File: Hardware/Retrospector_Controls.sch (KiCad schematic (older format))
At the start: 23 parts, among them J1 Audio_In_L, J10 Feedback_CV, J11 Audio_In_R, J12 Audio_Out_R, J13 Audio_Out_L, J2 Delay_CV_L, J3 Conn_01x08_Female, J4 Conn_01x08_Female, J5 Conn_01x08_Female, J6 Conn_01x08_Female, J7 Mix_CV, J8 Delay_CV_R, J9 Clock

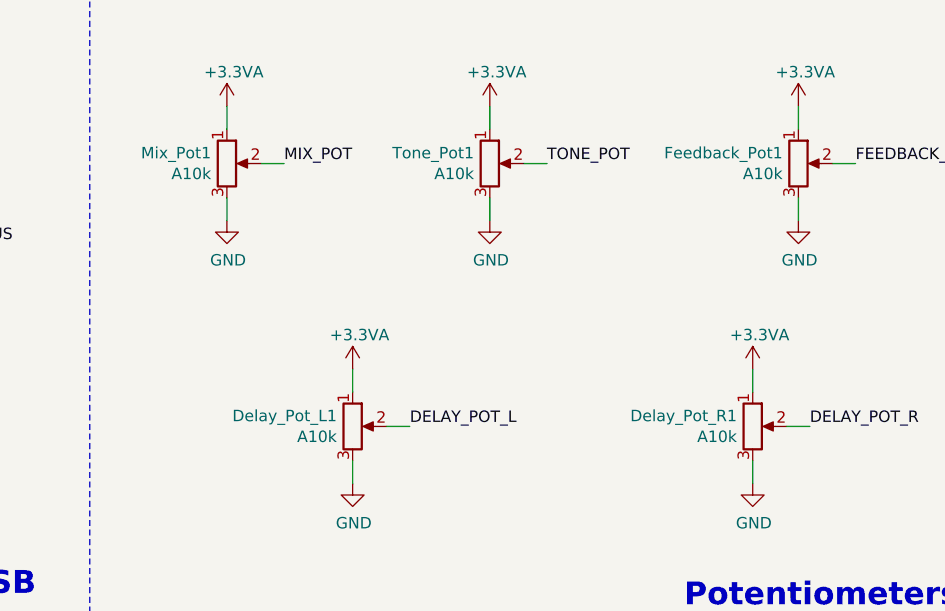
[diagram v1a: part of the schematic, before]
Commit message: Started updating schematics and pcb layout for rev 2 changes; updated and tested clock pin to use production assignment
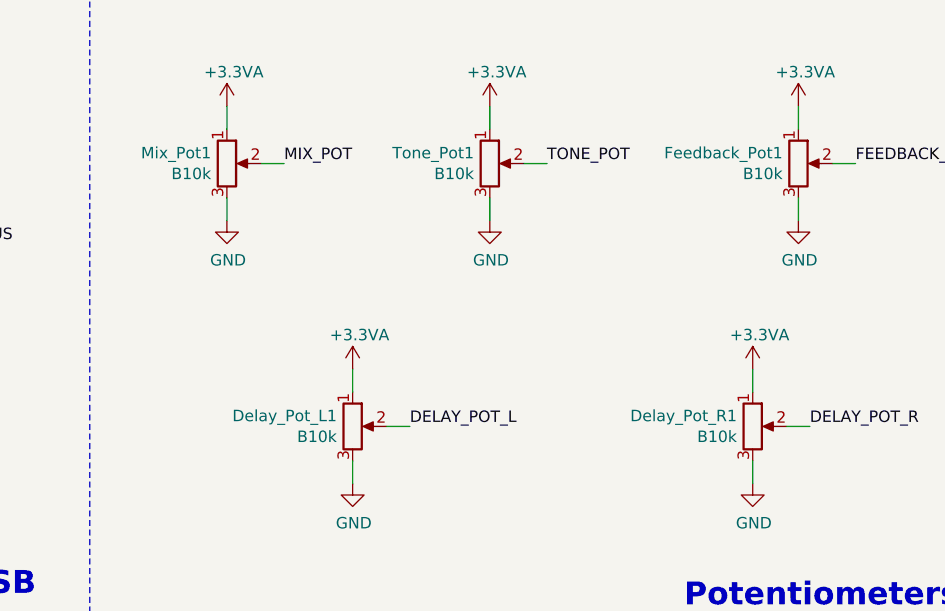
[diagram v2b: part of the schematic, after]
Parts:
- Delay_Pot_L1, Delay_Pot_R1, Feedback_Pot1, Mix_Pot1, Tone_Pot1: value A10k -> B10k
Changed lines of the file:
@@
 P 7800 4400
 F 0 "Mix_Pot1" H 7731 4446 50  0000 R CNN
-F 1 "A10k" H 7731 4355 50  0000 R CNN
+F 1 "B10k" H 7731 4355 50  0000 R CNN
 F 2 "Custom_Footprints:Alpha_9mm_Potentiometer" H 7800 4400 50  0001 C CNN
 F 3 "~" H 7800 4400 50  0001 C CNN
@@
 P 8950 4400
 F 0 "Tone_Pot1" H 8881 4446 50  0000 R CNN
-F 1 "A10k" H 8881 4355 50  0000 R CNN
+F 1 "B10k" H 8881 4355 50  0000 R CNN
 F 2 "Custom_Footprints:Alpha_9mm_Potentiometer" H 8950 4400 50  0001 C CNN
 F 3 "~" H 8950 4400 50  0001 C CNN
@@
 P 10300 4400
 F 0 "Feedback_Pot1" H 10231 4446 50  0000 R CNN
-F 1 "A10k" H 10231 4355 50  0000 R CNN
+F 1 "B10k" H 10231 4355 50  0000 R CNN
 F 2 "Custom_Footprints:Alpha_9mm_Potentiometer" H 10300 4400 50  0001 C CNN
 F 3 "~" H 10300 4400 50  0001 C CNN
@@
 P 8350 5550
 F 0 "Delay_Pot_L1" H 8281 5596 50  0000 R CNN
-F 1 "A10k" H 8281 5505 50  0000 R CNN
+F 1 "B10k" H 8281 5505 50  0000 R CNN
 F 2 "Custom_Footprints:Alpha_9mm_Potentiometer" H 8350 5550 50  0001 C CNN
 F 3 "~" H 8350 5550 50  0001 C CNN
@@
 P 10100 5550
 F 0 "Delay_Pot_R1" H 10031 5596 50  0000 R CNN
-F 1 "A10k" H 10031 5505 50  0000 R CNN
+F 1 "B10k" H 10031 5505 50  0000 R CNN
 F 2 "Custom_Footprints:Alpha_9mm_Potentiometer" H 10100 5550 50  0001 C CNN
 F 3 "~" H 10100 5550 50  0001 C CNN

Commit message: Started updating schematics for new revision
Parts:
- added D3: LED_LEFT, LEDs:LED_D5.0mm-4, symbol Device:LED_RABG
- added D4: LED_RIGHT, LEDs:LED_D5.0mm-4, symbol Device:LED_RABG
- added D5: LED_FILTER, LEDs:LED_D5.0mm-4, symbol Device:LED_RABG
- added J14: Filter, Custom_Footprints:THONKICONN_hole, symbol thonkiconn:AudioJack2_Ground_Switch
- added R1, R2, R3: 1k2, Resistors_SMD:R_0603_HandSoldering, symbol Device:R_Small
- added U1: TB62781FNG, Housings_SSOP:SSOP-20_4.4x6.5mm_Pitch0.65mm, symbol TB62781FNG:TB62781FNG
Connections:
- net labels added: +3.3V, +5V, FILTER_CV, LED_I2C_CLK, LED_I2C_DATA
- net labels removed: USB_DM, USB_DP, USB_VBUS
- wire segments 77 -> 126
- no-connect marks 5 -> 2
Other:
- note added: "LED Controller"
- note removed: "USB"
- moved on the sheet: J5, J6

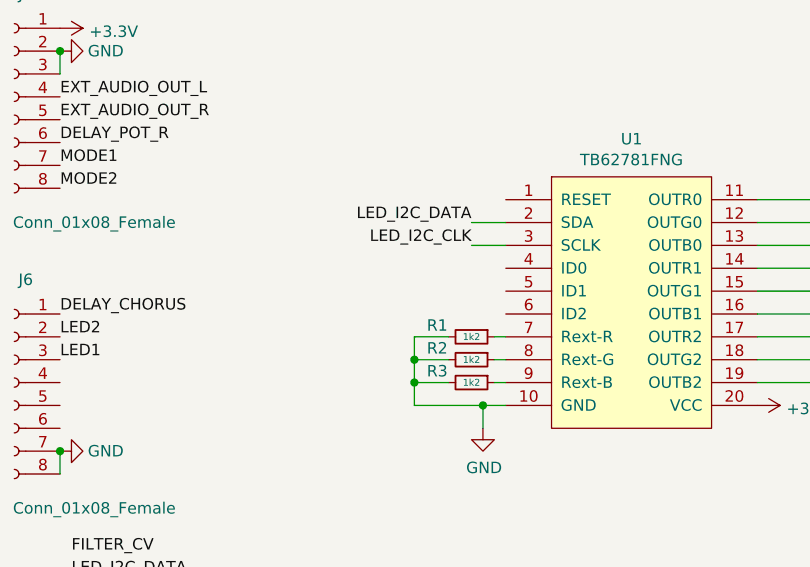
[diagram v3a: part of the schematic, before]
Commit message: Added some basic test code for initialising I2C
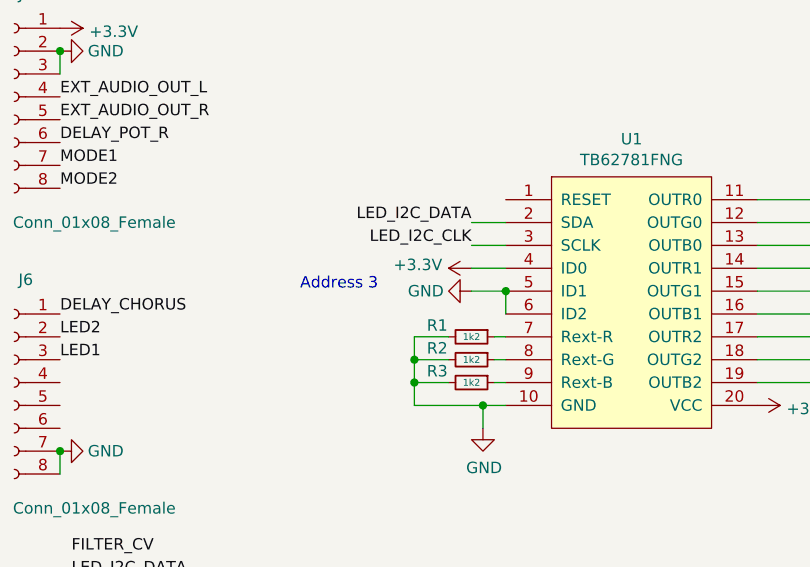
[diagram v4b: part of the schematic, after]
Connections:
- wire segments 126 -> 129
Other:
- note added: "Address 3"
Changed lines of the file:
@@
 Text Notes 4950 7400 0    100  ~ 20
 LED Controller
+$Comp
+L power:+3.3V #PWR?
+U 1 1 6015D1C1
+P 4300 5050
+F 0 "#PWR?" H 4300 4900 50  0001 C CNN
+F 1 "+3.3V" V 4315 5178 50  0000 L CNN
+F 2 "" H 4300 5050 50  0001 C CNN
+F 3 "" H 4300 5050 50  0001 C CNN
+	1    4300 5050
+	0    -1   -1   0
+$EndComp
+$Comp
+L power:GND #PWR?
+U 1 1 6015D81B
+P 4300 5150
+F 0 "#PWR?" H 4300 4900 50  0001 C CNN
+F 1 "GND" V 4300 4950 50  0000 C CNN
+F 2 "" H 4300 5150 50  0001 C CNN
+F 3 "" H 4300 5150 50  0001 C CNN
+	1    4300 5150
+	0    1    1    0
+$EndComp
+Wire Wire Line
+	4300 5150 4450 5150
+Wire Wire Line
+	4450 5250 4450 5150
+Connection ~ 4450 5150
+Wire Wire Line
+	4300 5050 4450 5050
+Text Notes 3550 5150 0    50   ~ 0
+Address 3
 $EndSCHEMATC

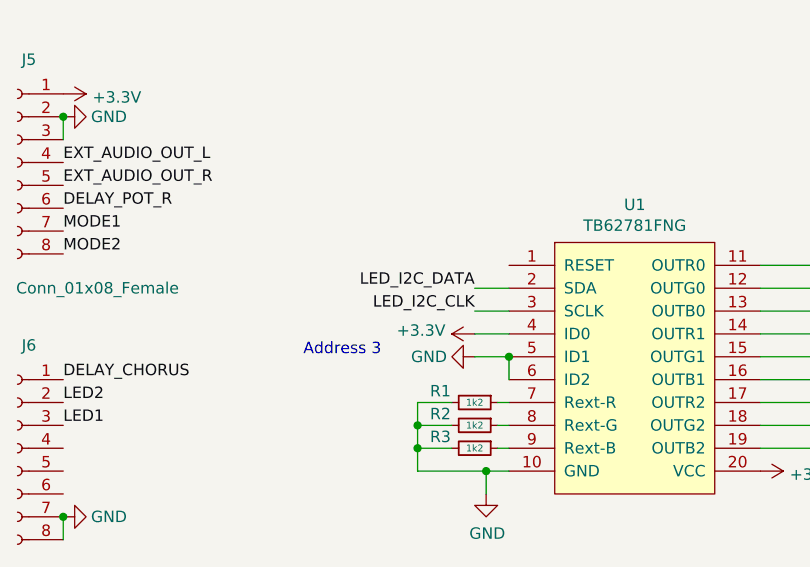
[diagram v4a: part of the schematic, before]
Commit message: Added some test code using SPI to control Toshiba LED controller
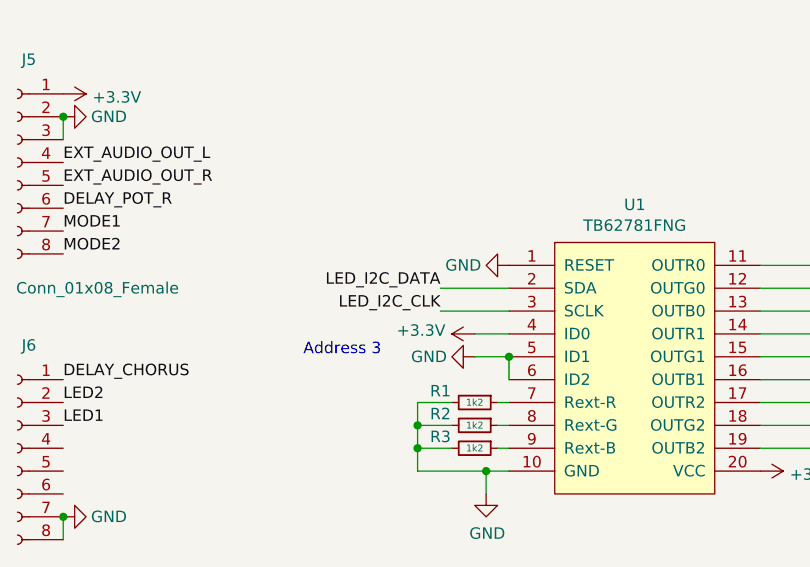
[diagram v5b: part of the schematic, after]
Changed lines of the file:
@@
 Wire Wire Line
 	4350 5650 4450 5650
-Text Label 4300 4850 2    50   ~ 0
+Text Label 4150 4850 2    50   ~ 0
 LED_I2C_DATA
-Text Label 4300 4950 2    50   ~ 0
+Text Label 4150 4950 2    50   ~ 0
 LED_I2C_CLK
 Text Label 2550 6400 0    50   ~ 0
@@
 	6700 6250 6650 6250
 Wire Wire Line
-	4300 4850 4450 4850
+	4150 4850 4450 4850
 Wire Wire Line
-	4300 4950 4450 4950
+	4150 4950 4450 4950
 $Comp
 L Device:R_Small R1
@@
 Text Notes 3550 5150 0    50   ~ 0
 Address 3
+$Comp
+L power:GND #PWR?
+U 1 1 6022D36C
+P 4450 4750
+F 0 "#PWR?" H 4450 4500 50  0001 C CNN
+F 1 "GND" V 4450 4550 50  0000 C CNN
+F 2 "" H 4450 4750 50  0001 C CNN
+F 3 "" H 4450 4750 50  0001 C CNN
+	1    4450 4750
+	0    1    1    0
+$EndComp
 $EndSCHEMATC

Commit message: Updated controls schematic
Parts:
- removed D1, D2: LED, LEDs:LED_D3.0mm, symbol Device:LED
- removed FXTYPE1: SW_SPST, Custom_Footprints:SPDTSubMiniature, symbol Switch:SW_SPST
- added FILTER_MODE1, WIDTH_MODE1: SW_SPDT_MSM, Custom_Footprints:SPDTSubMiniature, symbol Switch:SW_SPDT_MSM
- added LOCK1: SW_Push, Buttons_Switches_THT:SW_PUSH_6mm, symbol Switch:SW_Push
- R1, R2, R3: value 1k2 -> 3k3
- renumbered FXMODE1 to DELAY_MODE1, J3 to J1, J5 to J2, J4 to J3, J6 to J4, J1 to J5, J2 to J6
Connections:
- net labels added: CHORUS, HP_MODE, LED_SPI_CLK, LED_SPI_DATA, LOCK_BTN, LP_MODE, PINGPONG
- net labels removed: DELAY_CHORUS, LED1, LED2, LED_I2C_CLK, LED_I2C_DATA
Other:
- note removed: "Delay: Dual Mono, Ping Ping\nChorus: Chorus/Flange (w feedback?)"
- moved on the sheet: DELAY_MODE1

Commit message: Updates to control and panel PCBs
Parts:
- removed D3: LED_LEFT, LEDs:LED_D5.0mm-4, symbol Device:LED_RABG
- removed D4: LED_RIGHT, LEDs:LED_D5.0mm-4, symbol Device:LED_RABG
- removed D5: LED_FILTER, LEDs:LED_D5.0mm-4, symbol Device:LED_RABG
- added C1: 47uF, Capacitors_SMD:CP_Elec_5x5.8, symbol Device:CP_Small
- added D1, D2, D3: LED_RGBA, Custom_Footprints:LED_RGB_PLCC4, symbol Device:LED_RGBA
- DELAY_MODE1, FILTER_MODE1, WIDTH_MODE1: footprint Custom_Footprints:SPDTSubMiniature -> Custom_Footprints:SPDT_SubMiniature_Aligned
- Delay_Pot_L1, Delay_Pot_R1, Feedback_Pot1, Mix_Pot1, Tone_Pot1: footprint Custom_Footprints:Alpha_9mm_Potentiometer -> Custom_Footprints:Alpha_9mm_Potentiometer_Aligned
- LOCK1, RESET1: footprint Buttons_Switches_THT:SW_PUSH_6mm -> Custom_Footprints:SW_PUSH_6mm_aligned
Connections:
- net +5V: now also C1.1, D1.4 (A), D2.4 (A), D3.4 (A)
- net GND: now also C1.2
- net at U1.11 (OUTR0): now also D1.1 (RK)
- net at U1.12 (OUTG0): now also D1.2 (GK)
- net at U1.13 (OUTB0): now also D1.3 (BK)
- net at U1.14 (OUTR1): now also D2.1 (RK)
- net at U1.15 (OUTG1): now also D2.2 (GK)
- net at U1.16 (OUTB1): now also D2.3 (BK)
- net at U1.17 (OUTR2): now also D3.1 (RK)
- net at U1.18 (OUTG2): now also D3.2 (GK)
- net at U1.19 (OUTB2): now also D3.3 (BK)
- net LOCK_BTN renamed LINK_BTN
- net TONE_POT renamed FILTER_POT
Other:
- moved on the sheet: FILTER_MODE1, Feedback_Pot1, J1, J12, J2, J3, J4, R1, R2, R3, Tone_Pot1, U1
